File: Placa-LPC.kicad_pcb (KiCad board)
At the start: 2 copper layers, 120 x 90 mm, 49 parts, among them K1 CONN_3, K2 CONN_3, K3 CONN_3, K4 CONN_3, P1 12V, P10 CONN_6, P11 CONN_6, P13 CONN_2, P2 CONN_4, P3 CONN_4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

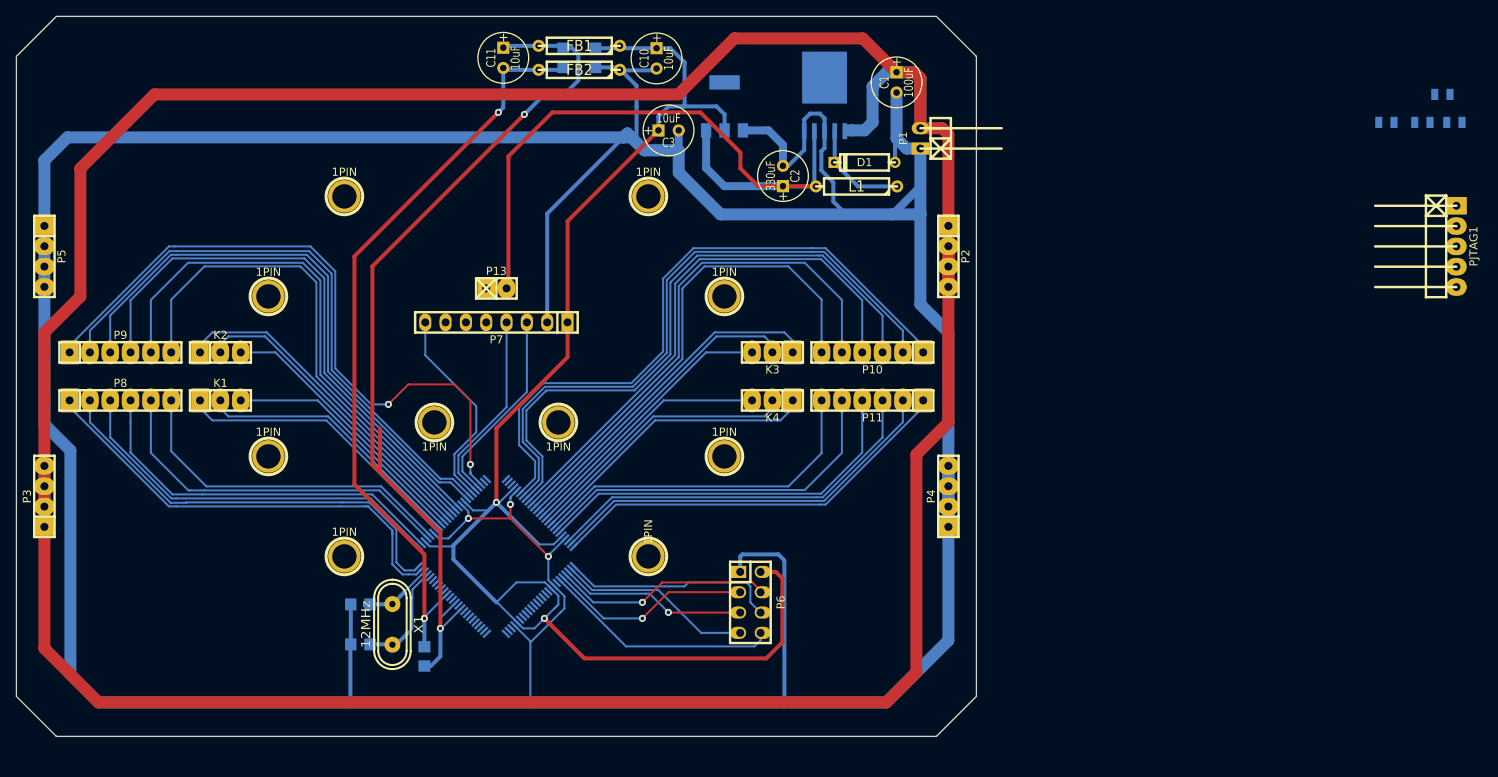
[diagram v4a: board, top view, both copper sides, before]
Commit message: Agregado de...
Pines programacion jtag e isp
Resistencias pull-up puerto cero de entrada.
ADC para bateria y reset
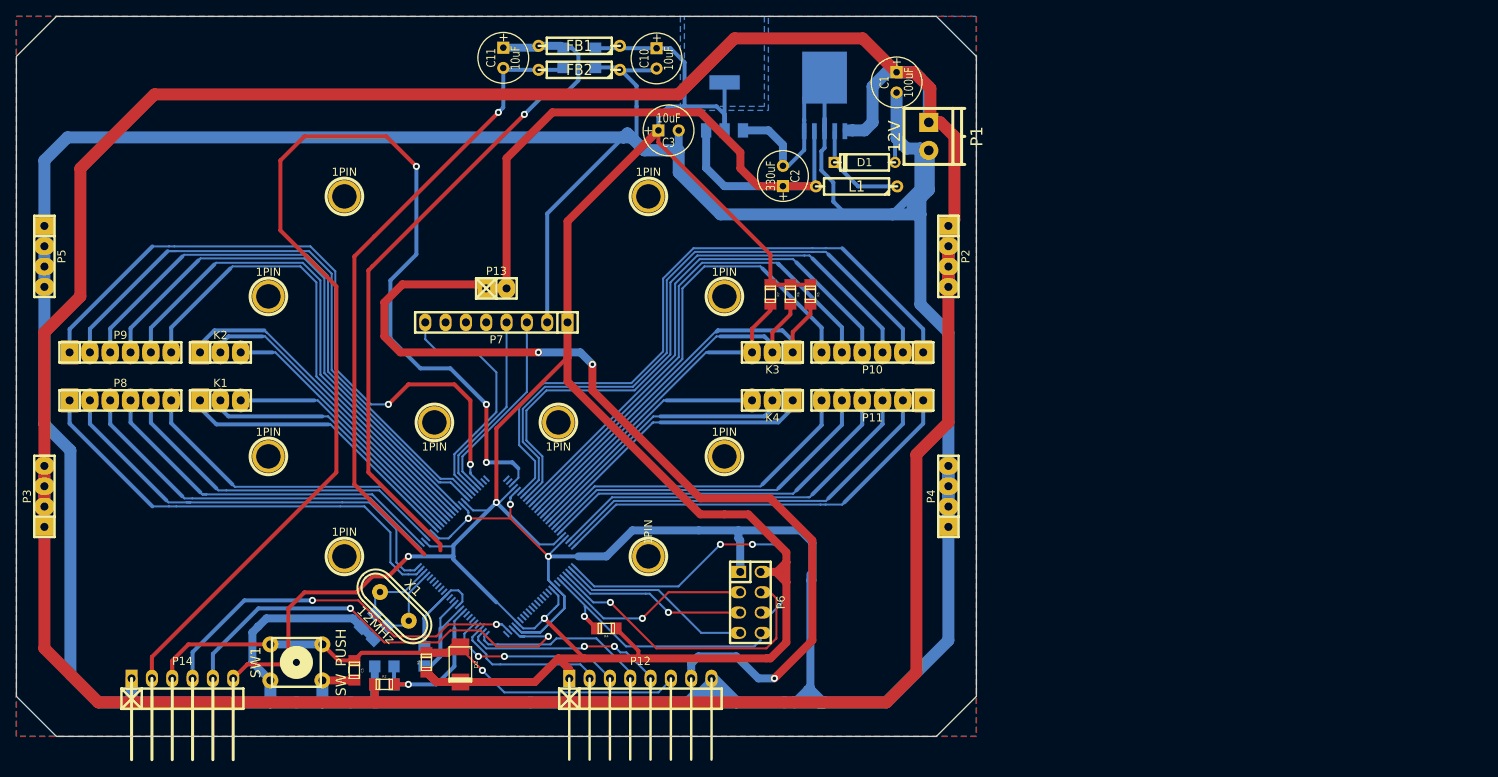
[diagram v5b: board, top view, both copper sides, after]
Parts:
- removed PJTAG1: CONN_5, pin_strip_5-90
- added C5: C, c_0805, F.Cu at (178.2, 163.8)
- added C6: C, c_0805, B.Cu at (182.0, 163.2)
- added D2: DIODE, do214ac, F.Cu at (191.5, 163.0)
- added P12: CONN_8, pin_strip_8-90, F.Cu at (214.0, 164.8)
- added P14: CONN_6, pin_strip_6-90, F.Cu at (156.8, 164.8)
- added R1: R, r_0805, F.Cu at (187.2, 162.8)
- added R2: R, r_0805, F.Cu at (182.0, 165.5)
- added R7: R, r_0805, F.Cu at (230.2, 116.8)
- added SW1: SW_PUSH, PCB_PUSH, F.Cu at (171.0, 162.8)
- P1: footprint pin_strip_2-90 -> pt_1,5-2-3,5-h
- R3: value 10k -> R; footprint SM0805 -> r_0805
- R4, R5, R6: value 10k -> R; footprint SM0805 -> r_0805; moved to F.Cu
- ULPC1: footprint TQFP-100 -> TQFP_100
- moved R3 151.4 mm to (182.0, 165.5)
- moved R4 120.0 mm to (209.8, 158.5), turned to 180 degrees
- moved R6 85.7 mm to (232.8, 116.8), turned to 270 degrees
- moved R5 75.1 mm to (235.2, 116.8), turned to 270 degrees
- moved C7 2.92 mm to (181.5, 159.0), turned to 45 degrees
- moved X1 2.26 mm to (183.2, 155.8), turned to 315 degrees
- moved C8 2.24 mm to (180.0, 157.5), turned to 45 degrees
- moved P1 1.77 mm to (250.8, 97.0)
- turned ULPC1 to 315 degrees
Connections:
- C1 pad 1: N-0000092 -> +12V
- K3 pad 1: N-0000022 -> N-0000092
- K3 pad 2: N-0000014 (its old number) -> N-0000090
- P1 pad 1: GND -> +12V
- P1 pad 2: N-0000092 -> GND
- P2 pad 1: N-0000092 -> +12V
- P2 pad 2: N-0000092 -> +12V
- P2 pad 3: N-0000092 -> +12V
- P2 pad 4: N-0000092 -> +12V
- P3 pad 1: N-0000092 -> +12V
- P3 pad 2: N-0000092 -> +12V
- P3 pad 3: N-0000092 -> +12V
- P3 pad 4: N-0000092 -> +12V
- P6 pad 8: N-000005 (its old number) -> N-0000025
- R3 pad 1: N-0000087 -> GND
- R3 pad 2: GND -> N-0000038
- R4 pad 2: N-0000086 -> N-0000025
- R5 pad 2: N-000006 (its old number) -> N-0000092
- R6 pad 2: N-0000010 (its old number) -> N-0000090
- U1 pad 1: N-0000092 -> +12V
- U1 pad 6: (no net) -> GND
- U3.1 pad 4: (no net) -> +3.3V
- ULPC1 pad 1: N-0000010 (its old number) -> N-0000035
- ULPC1 pad 100: N-0000087 -> (no net)
- ULPC1 pad 17: (no net) -> N-0000048
- ULPC1 pad 2: N-000006 (its old number) -> N-0000021
- ULPC1 pad 3: N-0000086 -> N-0000022
- ULPC1 pad 5: (no net) -> N-0000036
- ULPC1 pad 53: (no net) -> N-0000034
- ULPC1 pad 62: N-0000022 -> N-0000092
- ULPC1 pad 63: N-0000014 (its old number) -> N-0000090
- ULPC1 pad 81: N-000005 (its old number) -> N-0000025
- ULPC1 pad 9: (no net) -> N-0000038
- ULPC1 pad 98: (no net) -> N-0000033
- ULPC1 pad 99: (no net) -> N-0000031
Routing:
- net +12V: track 0.00 -> 410.9 mm
- net N-0000092: track 405.4 -> 51.5 mm
- net N-0000034: track 0.00 -> 271.8 mm, vias 0 -> 3
- net +3.3V: track 219.3 -> 416.5 mm, vias 2 -> 3
- net +5V: track 91.2 -> 246.2 mm, vias 0 -> 3
- net GND: track 624.3 -> 754.9 mm
- net N-0000033: track 0.00 -> 76.3 mm, vias 0 -> 2
- net N-0000048: track 0.00 -> 68.3 mm, vias 0 -> 1
- net N-0000031: track 0.00 -> 66.0 mm, vias 0 -> 2
- net N-0000090: track 0.00 -> 53.5 mm
- net N-0000014 (its old number): track 39.6 -> 0.00 mm
- net N-0000025: track 0.00 -> 35.4 mm, vias 0 -> 1
- net N-000005 (its old number): track 29.8 -> 0.00 mm
- net N-000009: track 84.3 -> 113.1 mm
- net N-0000021: track 0.00 -> 25.3 mm, vias 0 -> 2
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- added copper zone on B.Cu, net +3.3V
- added copper zone on B.Cu, net GND
- added copper zone on F.Cu, net GND

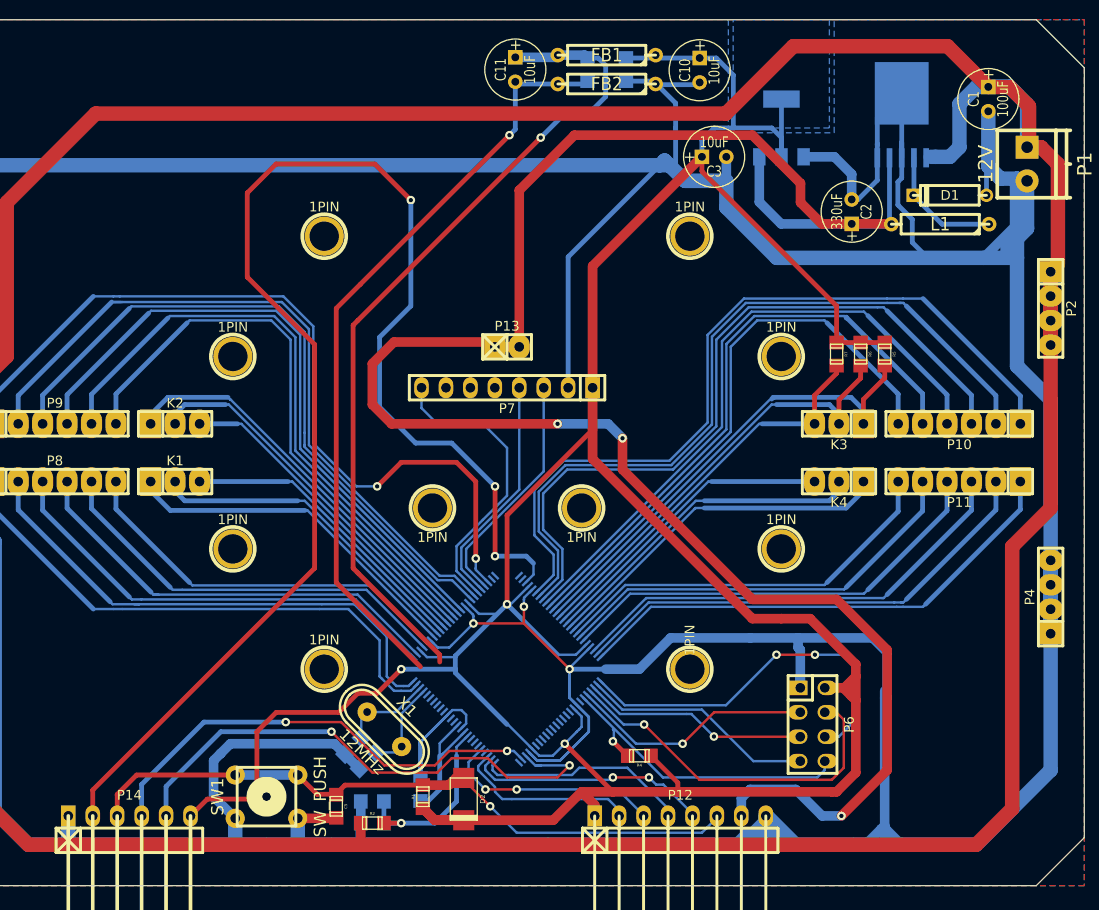
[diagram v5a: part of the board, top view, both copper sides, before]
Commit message: Version final
Agregado de resistencias pull up y cambio de pootprint lpc
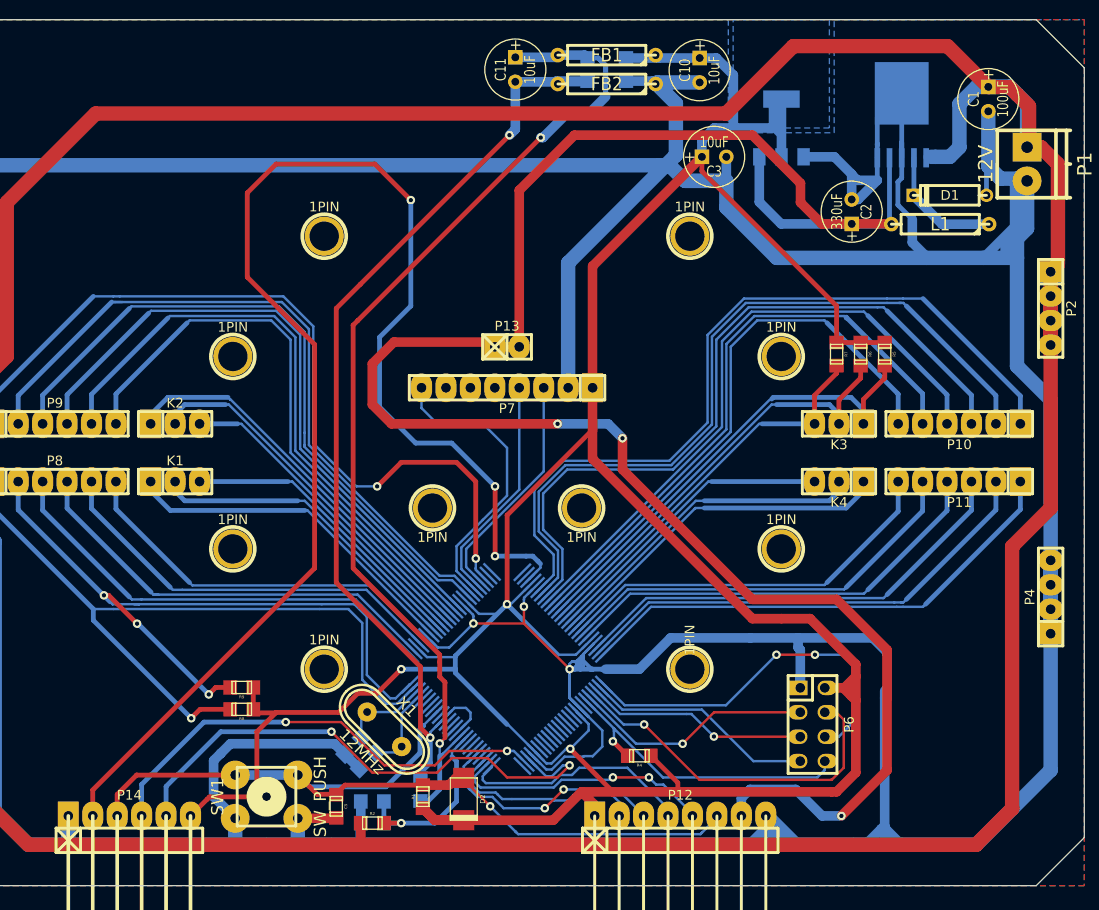
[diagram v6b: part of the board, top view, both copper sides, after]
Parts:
- added R8: R, r_0805, F.Cu at (168.4, 153.7)
- added R9: R, r_0805, F.Cu at (168.4, 151.4)
- ULPC1: footprint TQFP_100 -> TQFP_100_lpc
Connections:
- C5 pad 1: N-0000048 (its old number) -> N-0000051
- D2 pad 1: N-0000048 (its old number) -> N-0000051
- P12 pad 6: N-0000048 (its old number) -> N-0000051
- P14 pad 3: N-0000048 (its old number) -> N-0000051
- R1 pad 2: N-0000048 (its old number) -> N-0000051
- SW1 pad 2: N-0000048 (its old number) -> N-0000051
- ULPC1 pad 17: N-0000048 (its old number) -> N-0000051
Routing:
- net N-0000051: track 0.00 -> 113.2 mm, vias 0 -> 1
- net N-0000048 (its old number): track 68.3 -> 0.00 mm, vias 1 -> 0
- net GND: track 754.9 -> 819.3 mm
- net +3.3V: track 416.5 -> 455.5 mm
- net N-0000037: track 68.3 -> 100.9 mm, vias 0 -> 3
- net +3.3VADC: track 108.1 -> 138.2 mm, vias 1 -> 2
- net N-0000036: track 72.7 -> 98.0 mm, vias 0 -> 1
- net GNDA: track 99.5 -> 116.1 mm, vias 1 -> 2
- net (no net): track 6.50 -> 0.00 mm
- net N-0000019: track 19.3 -> 23.7 mm
- net N-0000093: track 13.1 -> 17.3 mm
- net N-0000018: track 25.3 -> 28.7 mm
- net N-0000050: track 23.2 -> 26.2 mm
- net N-0000039: track 22.2 -> 24.9 mm
- net N-0000031: track 271.8 -> 273.1 mm
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
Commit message: Deseño Crona
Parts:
- moved D2 109.6 mm to (90.2, 121.4), turned to 180 degrees
- moved C11 101.2 mm to (104.2, 46.5)
- moved C4 101.2 mm to (111.7, 46.5)
- moved C9 101.2 mm to (115.7, 46.5)
- moved FB1 101.2 mm to (113.7, 45.0)
- moved FB2 101.2 mm to (113.7, 48.0)
- moved R8 101.2 mm to (75.7, 113.0)
- moved 1PIN 101.2 mm to (122.3, 63.9)
- moved 1PIN 101.2 mm to (111.0, 92.1)
- moved 1PIN 101.2 mm to (131.8, 76.4)
- moved 1PIN 101.2 mm to (84.3, 63.9)
- moved 1PIN 101.2 mm to (74.8, 76.4)
- moved 1PIN 101.2 mm to (74.8, 96.4)
- moved 1PIN 101.2 mm to (84.3, 108.9)
- moved 1PIN 101.2 mm to (122.3, 108.9)
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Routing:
- net GND: track 819.3 -> 891.5 mm, vias 3 -> 4
- net N-0000031: track 273.1 -> 201.2 mm
- net +3.3VADC: track 138.2 -> 199.6 mm, vias 2 -> 4
- net GNDA: track 116.1 -> 176.3 mm, vias 2 -> 6
- net +3.3V: track 455.5 -> 492.6 mm, vias 3 -> 2
- net N-0000028: track 38.0 -> 70.0 mm
- net N-0000020: track 39.7 -> 61.0 mm
- net N-0000030: track 66.0 -> 85.8 mm
- net N-0000037: track 100.9 -> 84.2 mm
- net +5V: track 246.2 -> 258.3 mm
- net N-000001: track 47.6 -> 35.9 mm
- net N-0000042: track 52.3 -> 42.1 mm
- net N-0000014: track 30.9 -> 37.0 mm
- net N-0000039: track 24.9 -> 30.8 mm
- net N-0000027: track 23.6 -> 29.4 mm
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
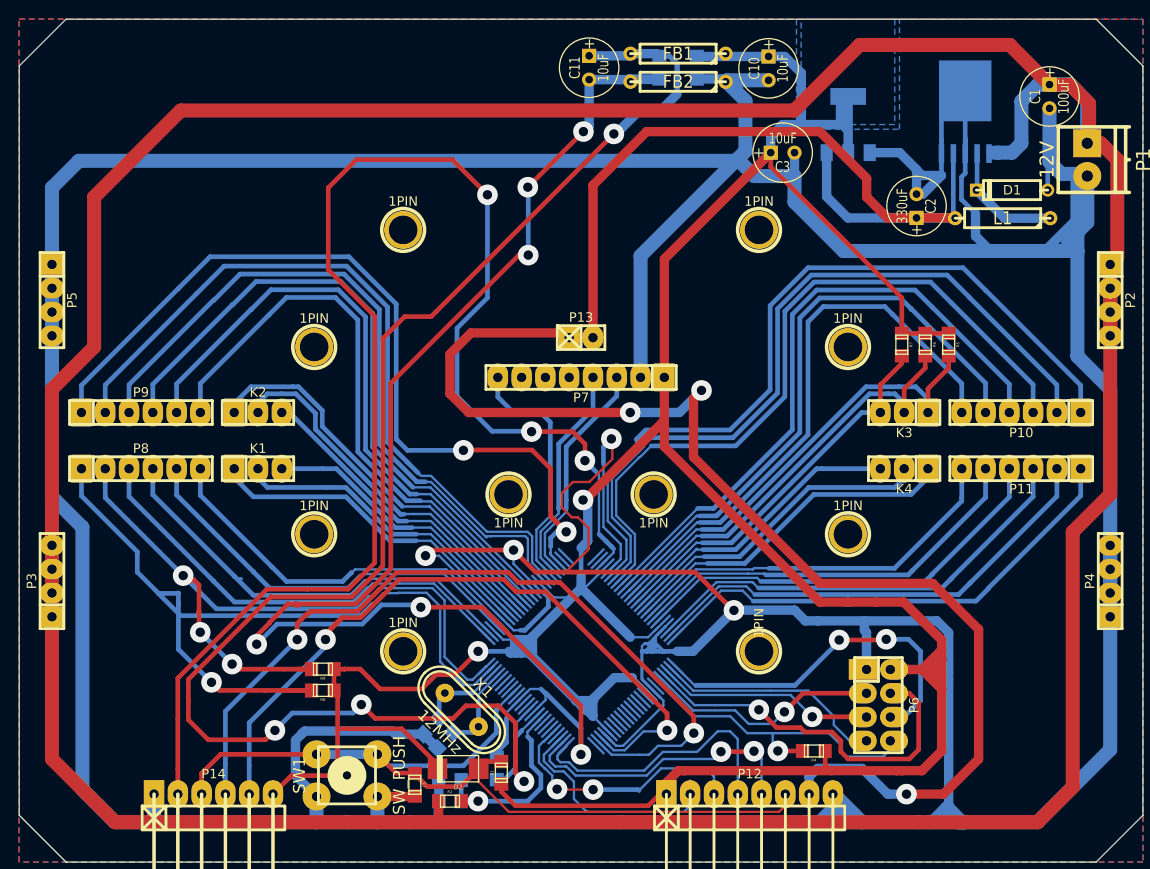
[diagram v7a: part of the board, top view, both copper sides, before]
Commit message: Ultimo diseño
Agregado de nombres y led smd
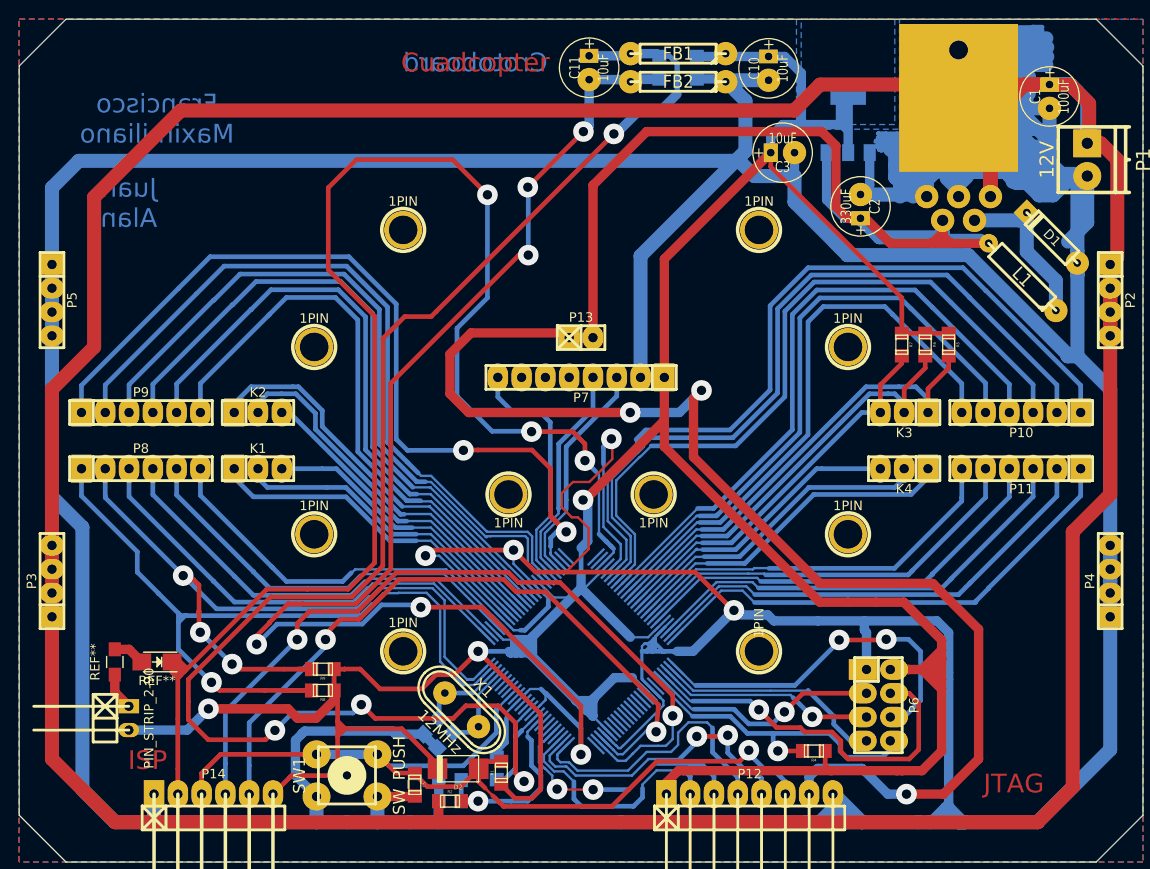
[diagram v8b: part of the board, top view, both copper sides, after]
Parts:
- removed U1: LM2575-5.0, d-pak-5
- added PIN_STRIP_2-90: Val**, w_pin_strip:pin_strip_2-90, F.Cu at (55.0, 116.0)
- added REF**: LED-1206, LEDs:LED-1206, F.Cu at (58.0, 110.0)
- added REF**: R_0805_HandSoldering, Resistors_SMD:R_0805_HandSoldering, F.Cu at (53.5, 110.0)
- added TO220-5-horiz: Q***, w_to:to220-5-horiz, B.Cu at (143.6, 52.3)
- moved D1 6.64 mm to (153.6, 64.7), turned to 135 degrees
- moved L1 6.60 mm to (150.4, 68.9), turned to 135 degrees
- moved C2 5.99 mm to (133.1, 61.4)
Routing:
- net GND: track 891.5 -> 1103.7 mm
- net +3.3V: track 492.6 -> 524.3 mm, vias 2 -> 3
- net N-0000024: track 35.0 -> 60.8 mm
- net +12V: track 410.9 -> 430.5 mm
- net (no net): track 0.00 -> 11.0 mm
- net N-0000021: track 25.0 -> 34.0 mm
- net N-0000051: track 113.6 -> 122.3 mm, vias 0 -> 1
- net N-0000031: track 201.2 -> 208.6 mm
- net N-0000019: track 27.1 -> 34.3 mm
- net N-0000036: track 92.7 -> 87.3 mm
- net N-0000039: track 30.8 -> 35.3 mm
- net N-0000029: track 28.5 -> 32.9 mm
- net N-0000018: track 33.1 -> 35.6 mm
- net N-0000035: track 79.2 -> 76.8 mm
- net +5V: track 258.3 -> 256.0 mm
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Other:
- board text added: "Crotoboard"
- board text added: "Cuadcopter"
- board text added: "Francisco Maximiliano"
- board text added: "ISP"
- board text added: "JTAG"
- board text added: "Juan Alan"
